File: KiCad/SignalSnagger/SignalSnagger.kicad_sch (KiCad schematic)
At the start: 58 parts, among them J102 Left, J104 Right, J105 36-5005-ND, J106 36-5006-ND, J107 36-5006-ND, J108 36-5005-ND, Q101 MMBT2222A, Q102 MMBT2222A, Q103 MMBT2222A, SW101 Sense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

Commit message: Ver 0.10
More schematic cleanup
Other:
- note added: "DF Antenna Module"
- note added: "Quadrature Sampling Detector"
- note added: "RF Amplifier"
- moved on the sheet: C101, C102, C103, C104, C105, C106, C107, C108, C109, C110, C111, C112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

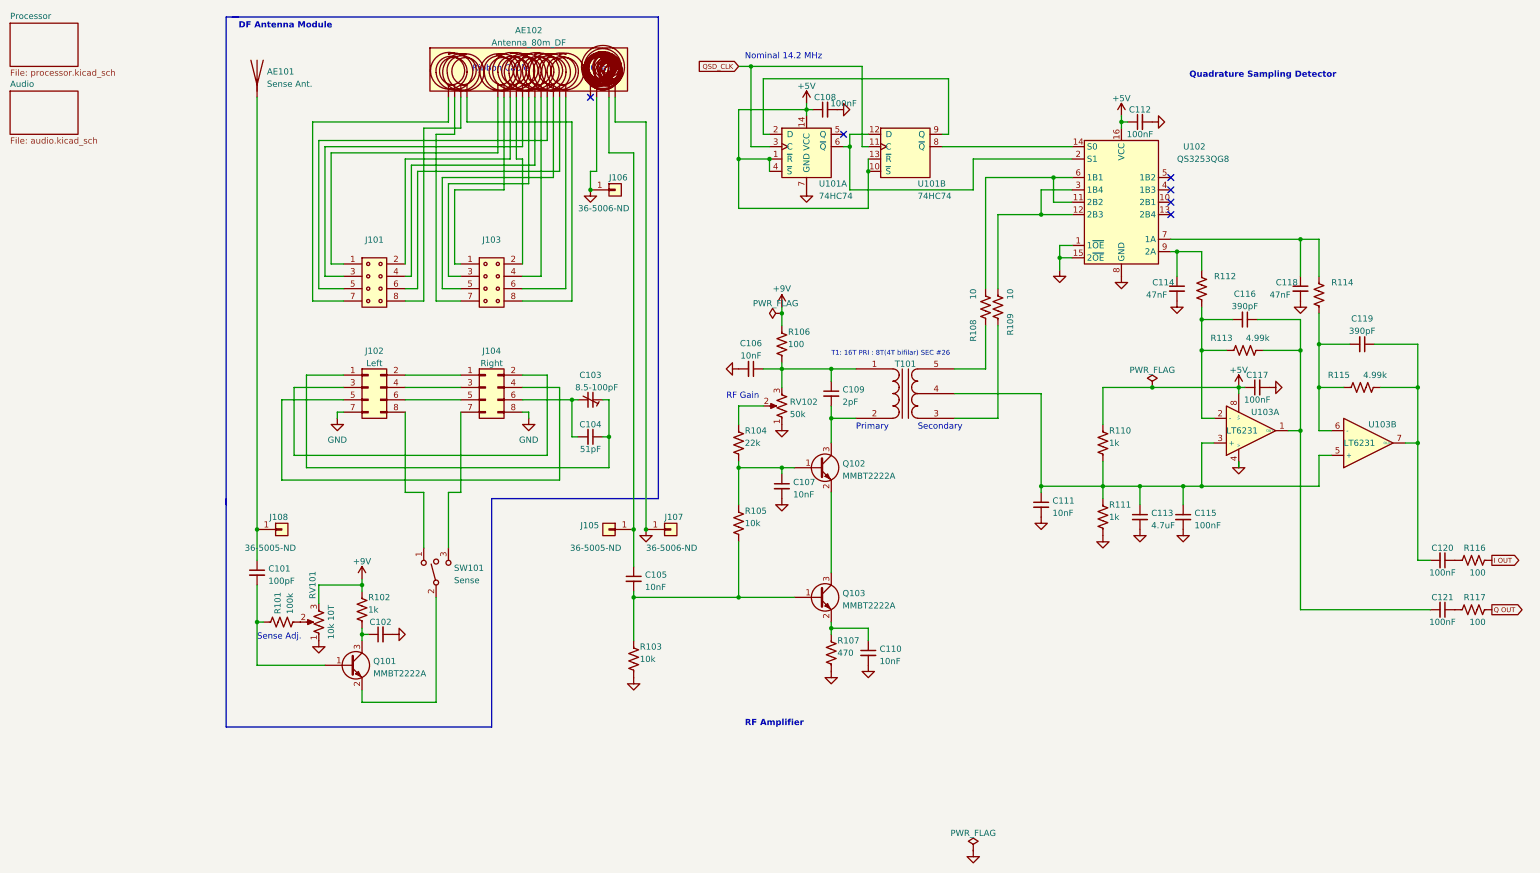
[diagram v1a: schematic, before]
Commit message: Rev 0.11
o Added missing DF loop center tap ground
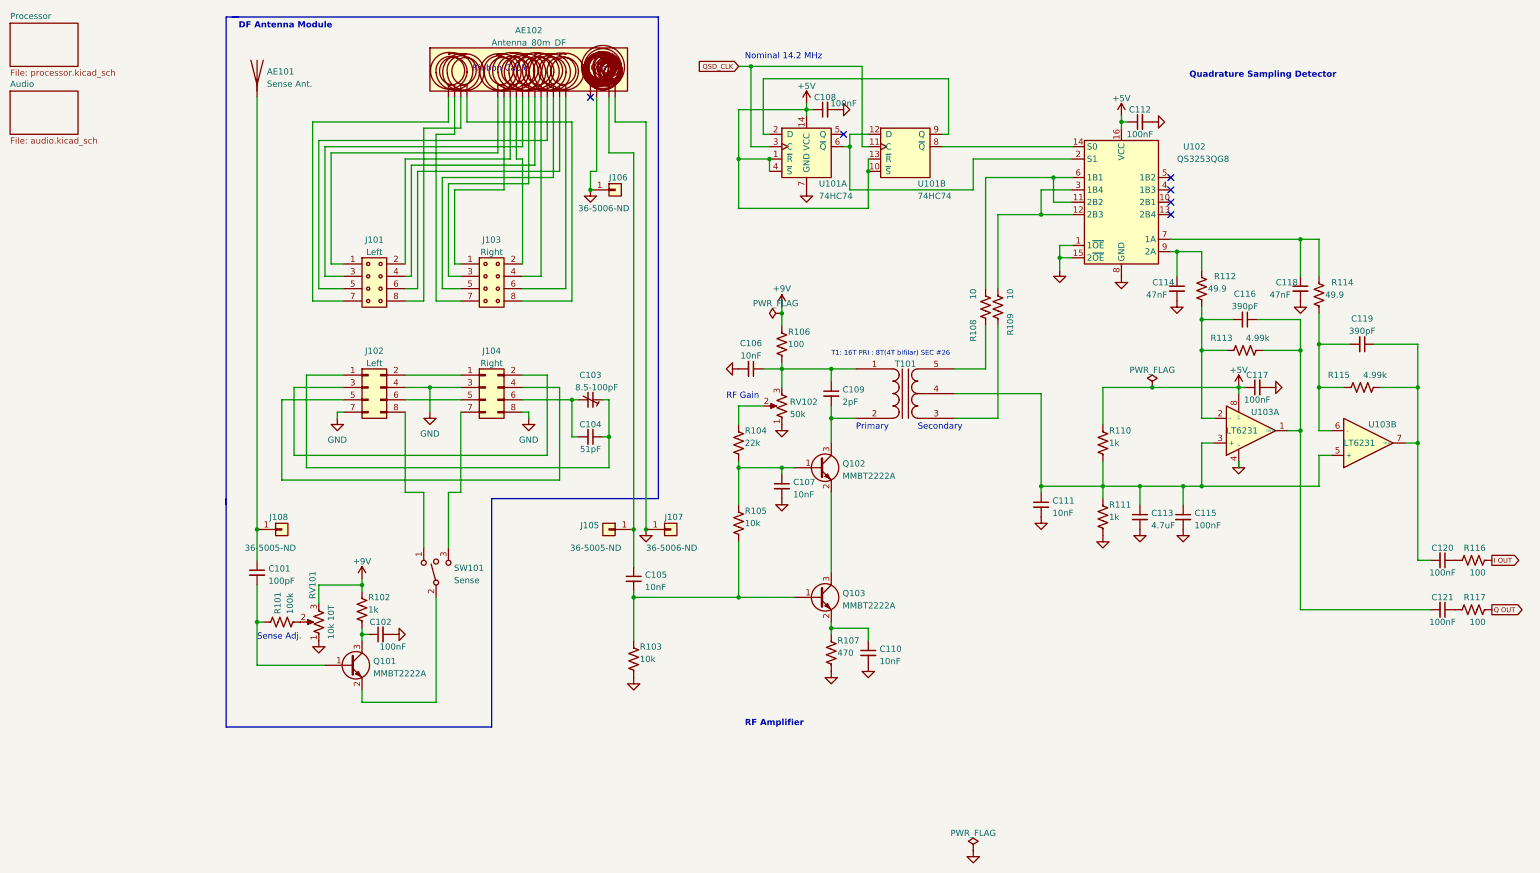
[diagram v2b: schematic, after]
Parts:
- C102: value (none) -> 100nF
- J101: value (none) -> Left
- J103: value (none) -> Right
- R112, R114: value (none) -> 49.9
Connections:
- net GND: now also J102.4 (Pin_4), J104.3 (Pin_3)
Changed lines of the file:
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@@
     (title "SignalSnagger")
     (date "2023-11-05")
-    (rev "0.10")
+    (rev "0.11")
   )
   (junction (at 195.58 113.03) (diameter 0) (color 0 0 0 0)
@@
   )
   (junction (at 129.54 109.22) (diameter 0) (color 0 0 0 0)
+  )
+  (junction (at 57.15 92.71) (diameter 0) (color 0 0 0 0)
   )
   (junction (at 143.51 43.18) (diameter 0) (color 0 0 0 0)
@@
     (stroke (width 0) (type default) (color 0 0 0 0))
   )
+  (wire (pts (xy 57.15 92.71) (xy 57.15 97.79))
+    (stroke (width 0) (type default) (color 0 0 0 0))
+  )
   (wire (pts (xy 83.82 92.71) (xy 76.2 92.71))
     (stroke (width 0) (type default) (color 0 0 0 0))
@@
     (stroke (width 0) (type default) (color 0 0 0 0))
   )
+  (wire (pts (xy 57.15 92.71) (xy 63.5 92.71))
+    (stroke (width 0) (type default) (color 0 0 0 0))
+  )
   (wire (pts (xy 218.44 99.06) (xy 215.9 99.06))
     (stroke (width 0) (type default) (color 0 0 0 0))
@@
     (stroke (width 0) (type default) (color 0 0 0 0))
   )
-  (wire (pts (xy 52.07 92.71) (xy 63.5 92.71))
+  (wire (pts (xy 52.07 92.71) (xy 57.15 92.71))
     (stroke (width 0) (type default) (color 0 0 0 0))
   )
@@
     (in_bom yes) (on_board yes) (fields_autoplaced)
     (property "Reference" "J101" (id 0) (at 45.72 62.3402 0))
-    (property "Value" "" (id 1) (at 45.72 64.8771 0))
+    (property "Value" "Left" (id 1) (at 45.72 64.8771 0))
     (property "Footprint" "" (id 2) (at 44.45 69.85 0)
       (effects (font (size 1.27 1.27)) hide)
@@
     (in_bom yes) (on_board yes)
     (property "Reference" "C102" (id 0) (at 46.99 140.97 90))
-    (property "Value" "" (id 1) (at 49.53 146.05 90))
+    (property "Value" "100nF" (id 1) (at 49.53 146.05 90))
     (property "Footprint" "" (id 2) (at 46.99 143.51 0)
       (effects (font (size 1.27 1.27)) hide)
@@
     )
     (property "Datasheet" "" (id 3) (at 210.82 74.93 0)
+      (effects (font (size 1.27 1.27)) hide)
+    )
+    (pin "1")
+  )
+  (symbol (lib_id "power:GND") (at 57.15 97.79 0) (unit 1)
+    (in_bom yes) (on_board yes) (fields_autoplaced)
+    (property "Reference" "#PWR?" (id 0) (at 57.15 104.14 0)
+      (effects (font (size 1.27 1.27)) hide)
+    )
+    (property "Value" "GND" (id 1) (at 57.15 102.2334 0))
+    (property "Footprint" "" (id 2) (at 57.15 97.79 0)
+      (effects (font (size 1.27 1.27)) hide)
+    )
+    (property "Datasheet" "" (id 3) (at 57.15 97.79 0)
       (effects (font (size 1.27 1.27)) hide)
     )
@@
       (effects (font (size 1.27 1.27)) (justify right))
     )
-    (property "Value" "" (id 1) (at 241.3 73.66 0)
+    (property "Value" "49.9" (id 1) (at 241.3 73.66 0)
       (effects (font (size 1.27 1.27)) (justify right))
     )
@@
       (effects (font (size 1.27 1.27)) (justify right))
     )
-    (property "Value" "" (id 1) (at 217.17 72.39 0)
+    (property "Value" "49.9" (id 1) (at 217.17 72.39 0)
       (effects (font (size 1.27 1.27)) (justify right))
     )
@@
     (in_bom yes) (on_board yes) (fields_autoplaced)
     (property "Reference" "J103" (id 0) (at 69.85 62.3402 0))
-    (property "Value" "" (id 1) (at 69.85 64.8771 0))
+    (property "Value" "Right" (id 1) (at 69.85 64.8771 0))
     (property "Footprint" "" (id 2) (at 68.58 69.85 0)
       (effects (font (size 1.27 1.27)) hide)
@@
       (reference "#PWR0310") (unit 1) (value "GND") (footprint "")
     )
+    (path "/7252cf63-d7d1-4028-b449-5792fc6d1955"
+      (reference "#PWR?") (unit 1) (value "GND") (footprint "")
+    )
     (path "/e51de444-614e-4b82-acb9-e91eb2e0cfb6"

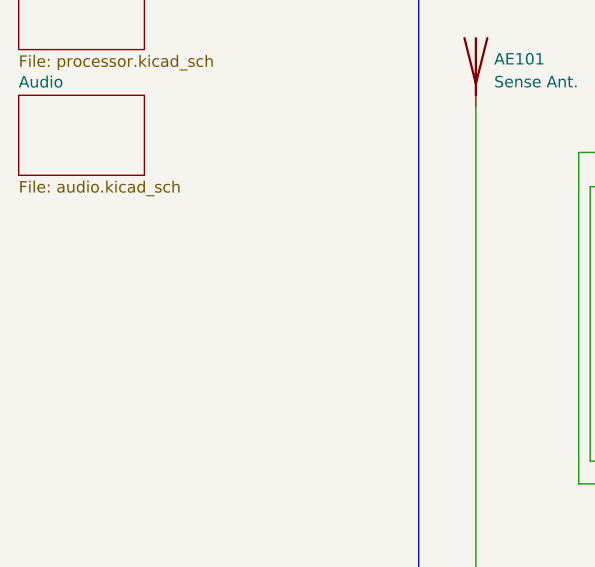
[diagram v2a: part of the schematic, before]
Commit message: Ver 0.12
Added antenna diagram sheet.
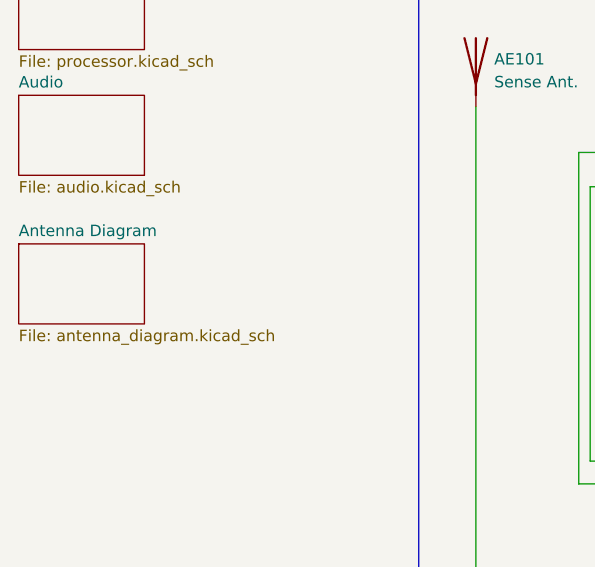
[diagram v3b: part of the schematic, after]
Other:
- added sheet Antenna Diagram (antenna_diagram.kicad_sch)
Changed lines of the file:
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@@
     (title "SignalSnagger")
     (date "2023-11-05")
-    (rev "0.11")
+    (rev "0.12")
   )
   (junction (at 195.58 113.03) (diameter 0) (color 0 0 0 0)
@@
     )
   )
+  (sheet (at -29.21 48.26) (size 13.97 8.89) (fields_autoplaced)
+    (stroke (width 0.1524) (type solid) (color 0 0 0 0))
+    (fill (color 0 0 0 0.0000))
+    (property "Sheet name" "Antenna Diagram" (id 0) (at -29.21 47.5484 0)
+      (effects (font (size 1.27 1.27)) (justify left bottom))
+    )
+    (property "Sheet file" "antenna_diagram.kicad_sch" (id 1) (at -29.21 57.7346 0)
+      (effects (font (size 1.27 1.27)) (justify left top))
+    )
+  )
   (sheet (at -29.21 17.78) (size 13.97 8.89) (fields_autoplaced)
     (stroke (width 0.1524) (type solid) (color 0 0 0 0))
@@
     (path "/b7e6c0d8-791a-469a-85d5-f8e886443224" (page "2"))
     (path "/109e0b43-3dac-4be2-a119-08b278e2e7f5" (page "3"))
+    (path "/a07b7207-b2ba-4964-b1bd-fe9eb7be7391" (page "4"))
   )
   (symbol_instances

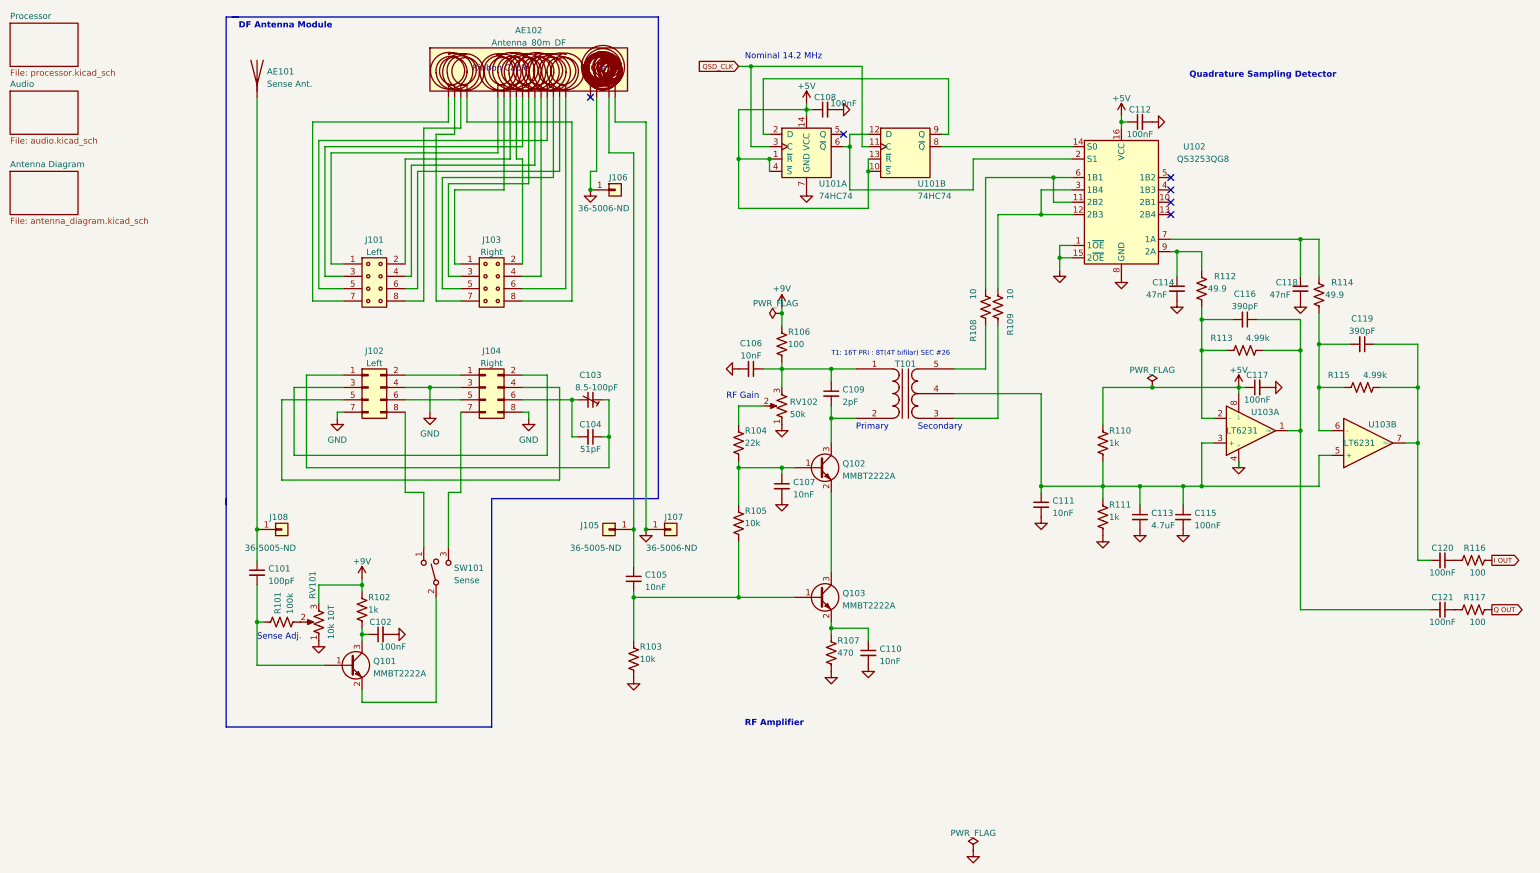
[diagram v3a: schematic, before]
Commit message: Ver 0.15
Schematic changes
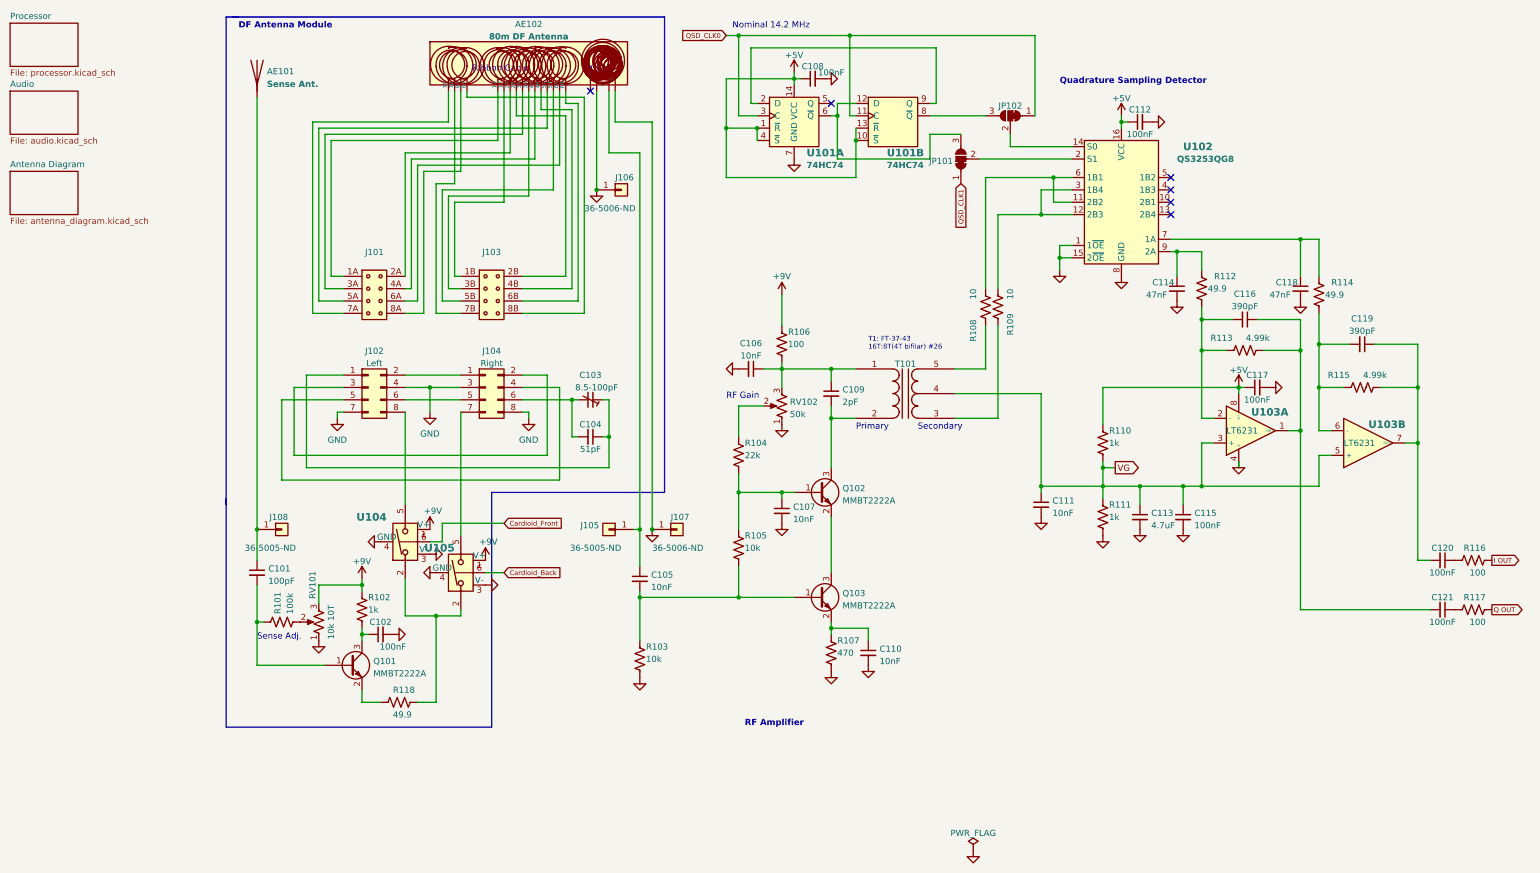
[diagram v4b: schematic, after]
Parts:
- removed SW101: Sense, symbol Switch:SW_SPDT_MSM
- added JP101: SolderJumper_3_Bridged12, symbol Jumper:SolderJumper_3_Bridged12
- added JP102: (no value), symbol Jumper:SolderJumper_3_Bridged12
- added R118: 49.9, symbol Device:R_US
- added U104, U105: (no value), Package_SO:TSOP-6_1.65x3.05mm_P0.95mm, symbol Analog_Switch:DG9422DV
- AE102: value Antenna_80m_DF -> 80m DF Antenna
- J101: value Left -> (none); Link (none) -> https://www.amazon.com/Pc-Accessories-Connectors-25-Pack-Co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
- J103: value Right -> (none); Link (none) -> https://www.amazon.com/Pc-Accessories-Connectors-25-Pack-Co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
- T101: Link (none) -> https://www.amidoncorp.com/ft-37-43/
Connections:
- net +9V: now also U104.1 (V+), U105.1 (V+)
- net GND: now also U104.3 (V-), U104.4 (GND), U105.3 (V-), U105.4 (GND)
- net VG: now reaches C111.1, C113.1, C115.1, R110.2, R111.1, T101.4 (SC), U103.3 (+), U103.5 (+)
- net at U102.14 (S0): now also JP102.2 (C); no longer U101.8 (~{Q})
- net at U101.12 (D), U101.6 (~{Q}): now also JP101.3 (B); no longer U102.2 (S1)
- net at J104.7 (Pin_7): now also U105.5
- net at Q101.2 (E): now also R118.2
- net at AE102.5 (1A): now also J101.1A (Pin_1); no longer J101.1 (Pin_1)
- net at AE102.7 (2A): now also J101.2A (Pin_2); no longer J101.2 (Pin_2)
- net at AE102.9 (3A): now also J101.3A (Pin_3); no longer J101.3 (Pin_3)
- net at AE102.11 (4A): now also J101.4A (Pin_4); no longer J101.4 (Pin_4)
- net at AE102.13 (5A): now also J101.5A (Pin_5); no longer J101.5 (Pin_5)
- net at AE102.15 (6A): now also J101.6A (Pin_6); no longer J101.6 (Pin_6)
- net at AE102.1 (7A): now also J101.7A (Pin_7); no longer J101.7 (Pin_7)
- net at AE102.3 (8A): now also J101.8A (Pin_8); no longer J101.8 (Pin_8)
- net at J102.8 (Pin_8): now also U104.5
- net at AE102.6 (1B): now also J103.1B (Pin_1); no longer J103.1 (Pin_1)
- net at AE102.8 (2B): now also J103.2B (Pin_2); no longer J103.2 (Pin_2)
- net at AE102.10 (3B): now also J103.3B (Pin_3); no longer J103.3 (Pin_3)
- net at AE102.12 (4B): now also J103.4B (Pin_4); no longer J103.4 (Pin_4)
- net at AE102.14 (5B): now also J103.5B (Pin_5); no longer J103.5 (Pin_5)
- net at AE102.16 (6B): now also J103.6B (Pin_6); no longer J103.6 (Pin_6)
- net at AE102.2 (7B): now also J103.7B (Pin_7); no longer J103.7 (Pin_7)
- net at AE102.4 (8B): now also J103.8B (Pin_8); no longer J103.8 (Pin_8)
- net QSD_CLK renamed QSD_CLK0
- net QSD_CLK0: now also JP102.1 (A)
- new net: JP101.2 (C), U102.2 (S1)
- new net: R118.1, U104.2, U105.2
- new net: JP102.3 (B), U101.8 (~{Q})
- new net Cardioid_Back: U105.6
- new net Cardioid_Front: U104.6
- new net QSD_CLK1: JP101.1 (A)
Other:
- note added: "T1: FT-37-43 16T:8T(4T bifilar) #26"
- note removed: "T1: 16T PRI : 8T(4T bifilar) SEC #26"
- moved on the sheet: C105, C107, C108, J101, J103, J106, J107, Q102, R103, R104, R105, U101A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
